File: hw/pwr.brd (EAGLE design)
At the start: 44.4 x 43.2 mm, 27 parts, among them IC1 MAX640, IC2 MAX640, IC3 MAX640

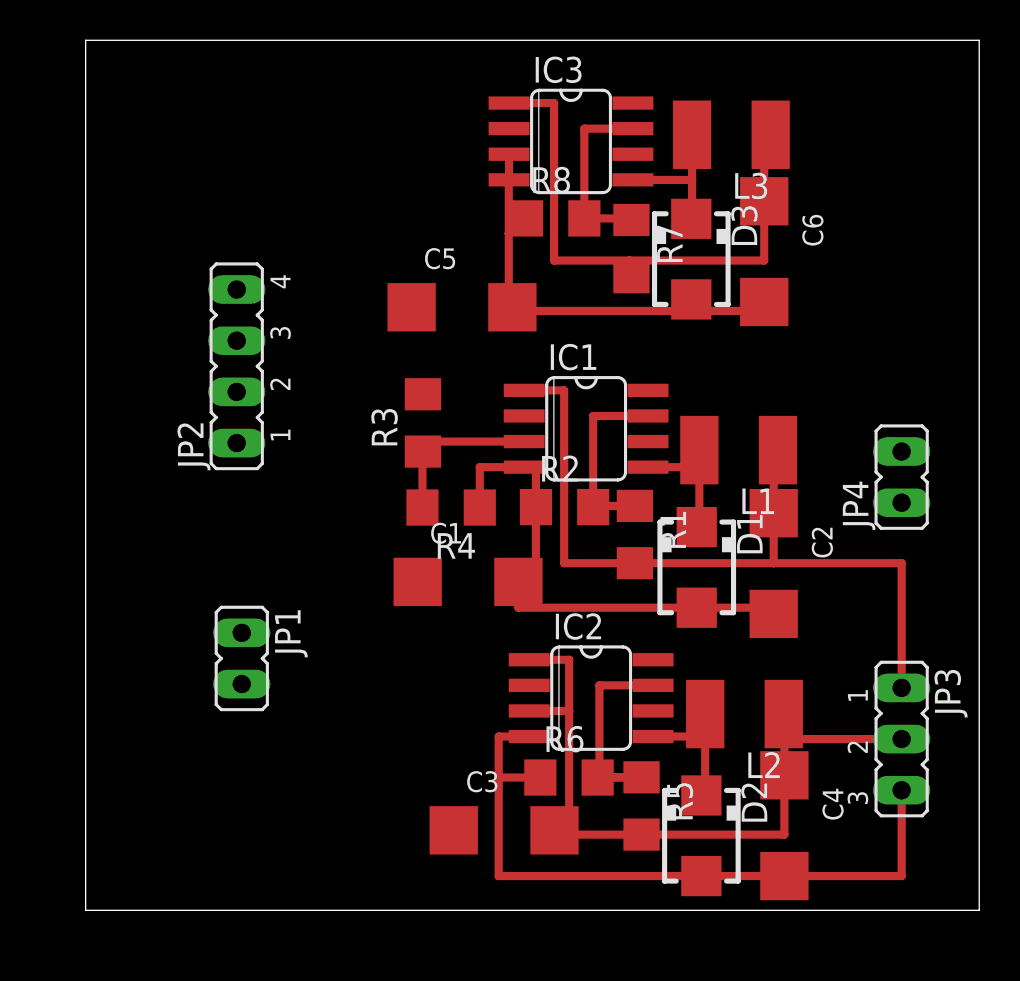
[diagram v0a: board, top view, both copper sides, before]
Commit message: created power board
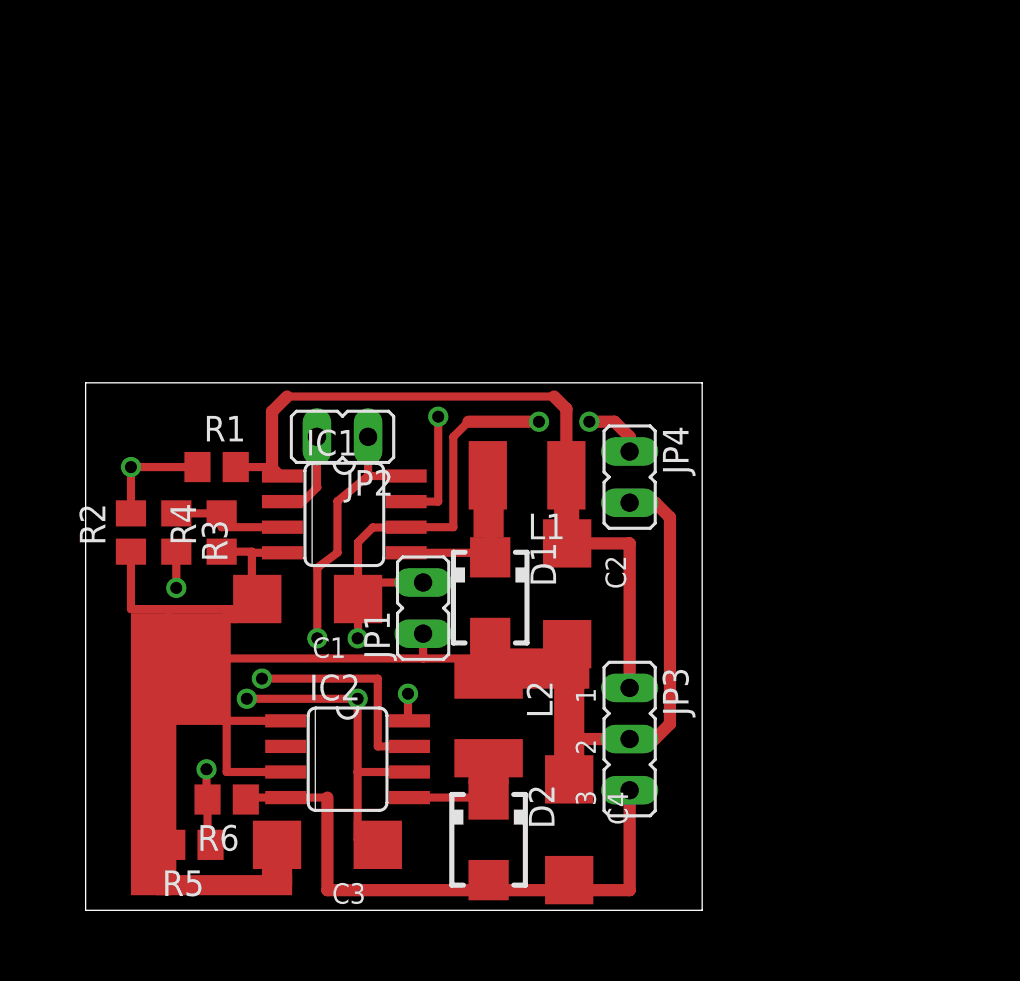
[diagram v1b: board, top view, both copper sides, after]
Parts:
- removed C5: 33u, rcl:SMC_C
- removed C6: 100u, rcl:SMC_C
- removed D3: SS14, mindspy:SMA
- removed IC3: MAX640, mindspy:SO08
- removed L3: (no value), rcl:L1812
- removed R7, R8: (no value), rcl:R1206
- JP2: value CTRL -> (none); device jumper:JP4 -> jumper:JP1
- R1, R2, R3, R4, R5, R6: device rcl:R1206 -> rcl:R0805
- moved R5 22.4 mm to (5.25, 3.25), turned to 180 degrees
- moved R2 21.6 mm to (2.25, 18.8), turned to 90 degrees
- moved R1 21.0 mm to (6.50, 22.0), turned to 0 degrees
- moved R6 17.0 mm to (7.00, 5.50), turned to 180 degrees
- moved JP3 13.5 mm to (27.0, 8.50)
- moved JP4 13.5 mm to (27.0, 21.5), turned to 180 degrees
- moved R3 13.4 mm to (4.50, 18.8), turned to 270 degrees
- moved IC1 12.7 mm to (12.8, 19.6)
- moved L2 12.7 mm to (20.0, 9.50), turned to 270 degrees
- moved IC2 12.5 mm to (13.0, 7.50)
- moved R4 11.5 mm to (6.75, 18.8), turned to 90 degrees
- moved C4 10.7 mm to (24.0, 4.00)
- moved L1 10.6 mm to (21.9, 21.6)
- moved D2 10.6 mm to (20.0, 3.50)
- moved C2 10.4 mm to (23.9, 15.7)
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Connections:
- removed net +5V: C1.+, C3.+, C5.+, IC1.6, IC2.6, IC3.6, JP1.2, R3.2
- removed net 3V3: C6.+, IC3.1, JP4.1, L3.1, R7.2
- removed net N$11: IC2.8, JP2.2
- removed net N$13: IC3.7, R7.1, R8.2
- removed net N$14: IC3.8, JP2.1
- removed net N$2: IC1.8, JP2.3
- removed net N$3: IC1.2, JP2.4
- removed net N$9: D3.C, IC3.5, L3.2
- new net LBO: IC1.2, JP2.2
- new net SHDN: IC1.8, IC2.8, JP2.1
- new net VBAT: C1.+, C3.+, IC1.6, IC2.6, JP1.2, JP4.1, R3.2
- net GND: no longer C5.-, C6.-, D3.A, IC3.3, IC3.4, R8.1
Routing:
- net VBAT: track 0.00 -> 43.9 mm, vias 0 -> 6
- net 3V3: track 28.0 -> 0.00 mm
- net SHDN: track 0.00 -> 14.5 mm, vias 0 -> 2
- net N$13: track 9.28 -> 0.00 mm
- net GND: track 84.9 -> 93.0 mm
- net N$9: track 7.15 -> 0.00 mm
- net -2V5: track 35.2 -> 29.7 mm
- net LBO: track 0.00 -> 4.54 mm
- net N$10: track 11.5 -> 14.5 mm, vias 0 -> 2
- net N$1: track 6.50 -> 9.02 mm
- net N$6: track 8.32 -> 5.95 mm
- net N$8: track 9.38 -> 11.4 mm, vias 0 -> 2
- net +2V5: track 39.3 -> 37.4 mm
- net N$4: track 6.82 -> 5.98 mm
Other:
- board size 44.4 x 43.2 mm -> 30.6 x 26.2 mm
- board text added: "+2V5"
- board text added: "-2V5"
- board text added: "AGND"
- board text added: "BAT+"
- board text added: "DGND"
- board text added: "LBO"
- board text added: "MindSpy.org"
- board text added: "SHDN"
- board text added: "VBAT"
- board text added: "pwr board ver. 0.1"

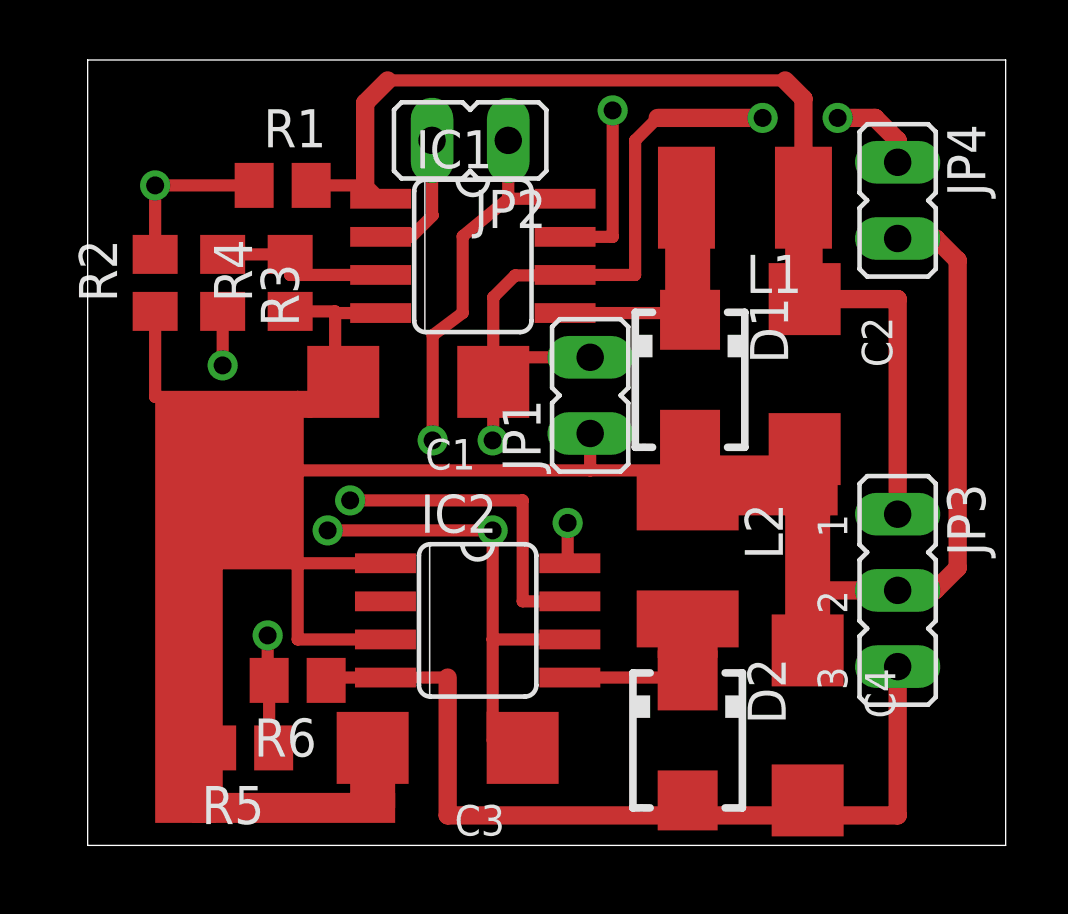
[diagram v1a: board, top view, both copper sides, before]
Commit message: Fix problems with polarity and route length and crossing  as well
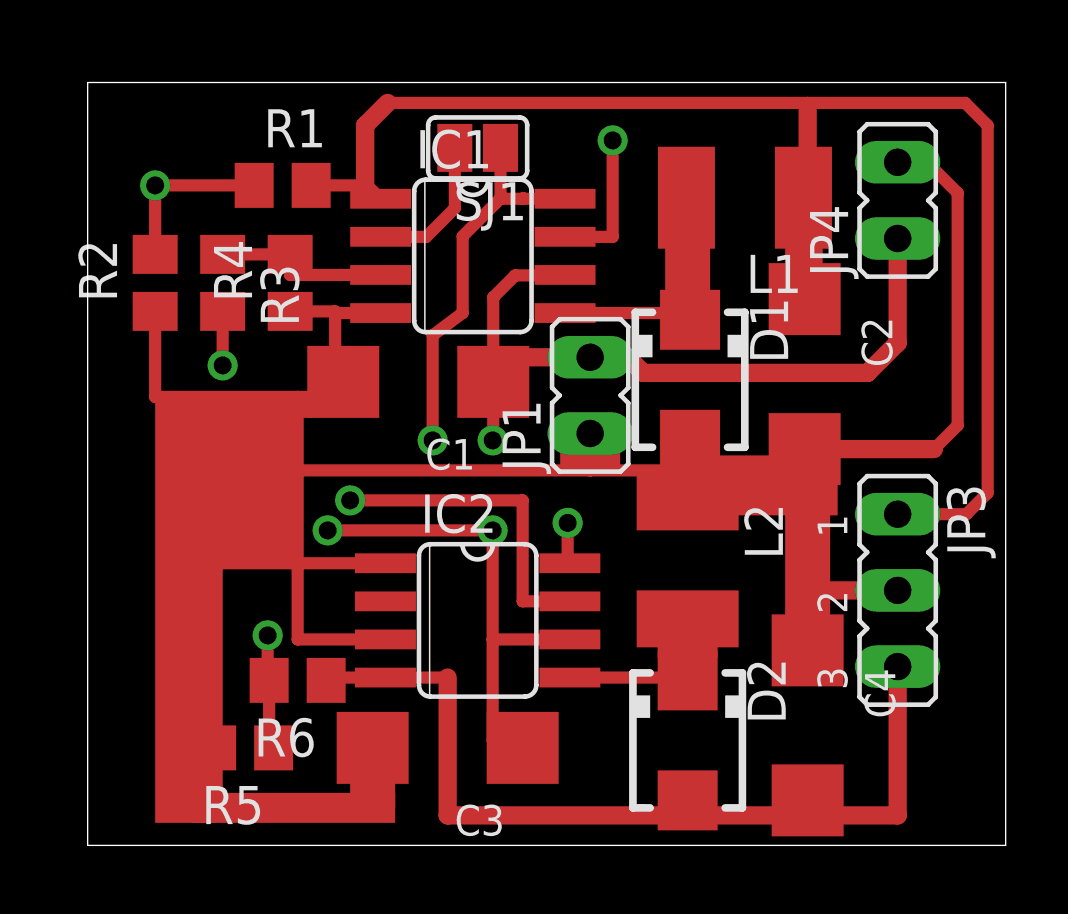
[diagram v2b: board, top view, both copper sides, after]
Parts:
- removed JP2: (no value), jumper:JP1
- added SJ1: (no value), jumper:SJ
- turned JP4 to 0 degrees
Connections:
- net LBO: now also SJ1.2; no longer JP2.2
- net SHDN: now also SJ1.1; no longer JP2.1
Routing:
- net +2V5: track 37.4 -> 48.1 mm
- net N$8: track 11.4 -> 10.4 mm
- net GND: track 93.0 -> 93.7 mm
- net VBAT: track 43.9 -> 43.8 mm, vias 6 -> 4
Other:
- board size 30.6 x 26.2 mm -> 30.6 x 25.4 mm

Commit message: Sargon rocks
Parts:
- removed SJ1: (no value), jumper:SJ
- L1, L2: device rcl:L1812 -> rcl:POWER-CHOKE_WE-TPC
- moved JP1 15.4 mm to (2.25, 20.2)
- moved C3 13.4 mm to (2.75, 13.0), turned to 90 degrees
- moved R1 13.1 mm to (19.5, 20.5), turned to 90 degrees
- moved D2 12.5 mm to (26.8, 14.0), turned to 90 degrees
- moved R4 11.6 mm to (16.5, 25.0), turned to 180 degrees
- moved R3 10.4 mm to (12.8, 25.0), turned to 180 degrees
- moved JP3 9.00 mm to (36.0, 8.50)
- moved JP4 9.00 mm to (36.0, 21.5)
- moved C4 8.61 mm to (31.8, 7.75)
- moved C2 7.85 mm to (31.6, 17.0)
- moved R2 7.76 mm to (9.75, 20.8), turned to 270 degrees
- moved R6 6.86 mm to (10.8, 11.2), turned to 270 degrees
- moved R5 6.66 mm to (10.8, 7.00), turned to 270 degrees
- moved L2 6.36 mm to (24.5, 5.00)
- moved C1 4.24 mm to (7.55, 13.0), turned to 270 degrees
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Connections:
- removed net LBO: IC1.2, SJ1.2
- net SHDN: no longer SJ1.1
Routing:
- net GND: track 93.7 -> 0.00 mm
- net VBAT: track 43.8 -> 90.9 mm, vias 4 -> 0
- net N$4: track 5.98 -> 24.5 mm
- net +2V5: track 48.1 -> 32.7 mm
- net -2V5: track 29.7 -> 44.6 mm
- net SHDN: track 14.3 -> 3.29 mm
- net N$1: track 9.02 -> 16.0 mm
- net LBO: track 4.88 -> 0.00 mm
- net N$10: track 14.5 -> 10.1 mm, vias 2 -> 0
- net N$8: track 10.4 -> 13.2 mm, vias 2 -> 0
- net N$6: track 5.95 -> 4.17 mm
- added copper zone on layer 1, net GND
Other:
- board size 30.6 x 25.4 mm -> 40.4 x 29.7 mm
- board text removed: "+2V5"
- board text removed: "-2V5"
- board text removed: "AGND"
- board text removed: "DGND"
- board text removed: "LBO"
- board text removed: "SHDN"
- board text removed: "VBAT"
